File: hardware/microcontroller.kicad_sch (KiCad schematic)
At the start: 8 parts, among them U1 STM32G474QBT6

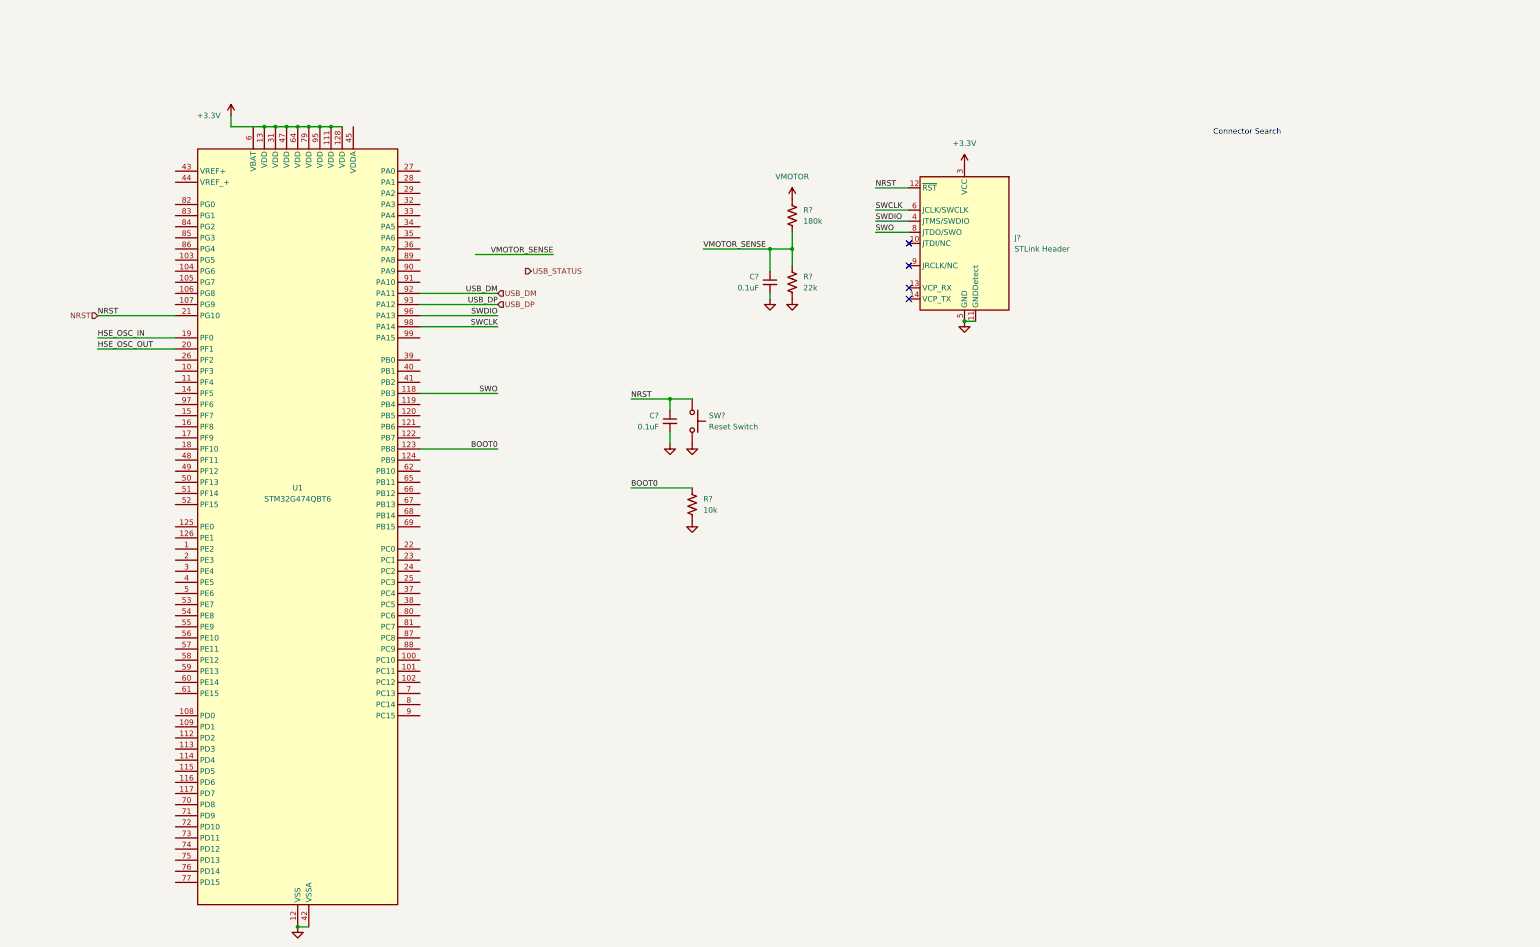
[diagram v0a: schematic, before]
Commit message: SD Card Pull Ups and ESD
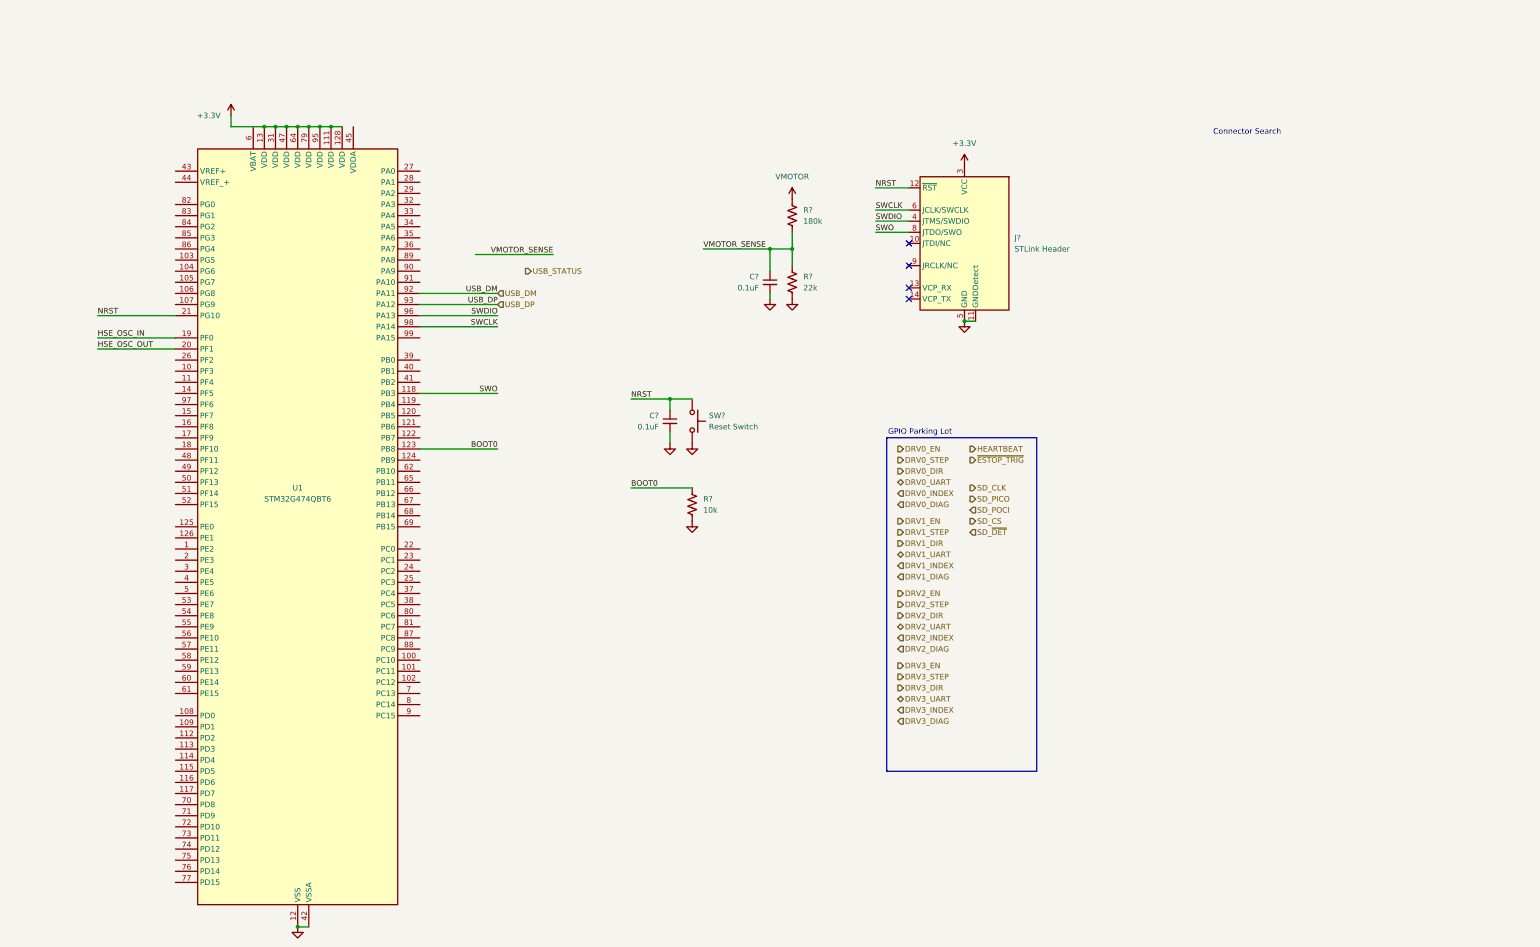
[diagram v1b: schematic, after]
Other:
- note added: "GPIO Parking Lot"

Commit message: Fixes and STM32 Pin Assignment Notes
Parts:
- removed SW?: Reset Switch, Button_Switch_SMD:SW_SPST_PTS647_Sx38, symbol Switch:SW_Push
- added D?: BAT54S, Package_TO_SOT_SMD:SOT-23, symbol Diode:BAT54S
- added R? (x5): 10k, Resistor_SMD:R_0603_1608Metric, symbol Device:R_US
- added SW?: USER3, Button_Switch_SMD:SW_SPST_PTS645Sx43SMTR92, symbol Switch:SW_Push
- added SW?: USER1, Button_Switch_SMD:SW_SPST_PTS645Sx43SMTR92, symbol Switch:SW_Push
- added SW?: USER0, Button_Switch_SMD:SW_SPST_PTS645Sx43SMTR92, symbol Switch:SW_Push
- added SW?: BOOT, Button_Switch_SMD:SW_SPST_PTS645Sx43SMTR92, symbol Switch:SW_Push
- added SW?: USER2, Button_Switch_SMD:SW_SPST_PTS645Sx43SMTR92, symbol Switch:SW_Push
- added SW?: RESET, Button_Switch_SMD:SW_SPST_PTS645Sx43SMTR92, symbol Switch:SW_Push
- C?: value 0.1uF -> 1nF; Part Number CC0603KRX7R9BB104 -> C0603C102K5RACTU; Vendor URL https://www.digikey.com/en/products/detail/yageo/CC0603KRX7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 -> https://www.digikey.com/en/products/detail/kemet/C0603C102K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
- J?: footprint Connector_PinHeader_1.27mm:PinHeader_2x07_P1.27mm_Vertical -> Connector_PinHeader_1.27mm:PinHeader_2x07_P1.27mm_Vertical_SMD; Part Number 3220-14-0100-00 -> FTSH-107-01-L-DV-K-P-TR; Vendor URL https://www.digikey.com/en/products/detail/cnc-tech/3220-14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 -> https://www.digikey.com/en/products/detail/samtec-inc/FTSH-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
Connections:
- net +3.3V: now also U1.6 (VBAT), D?.2 (K), R?.1, R?.1, R?.1, R?.1, R?.1, SW?.1
- net BOOT0: now also SW?.2
- net GND: now also D?.1 (A), SW?.2, SW?.2, SW?.2, SW?.2, SW?.2
- net NRST: now also R?.2, SW?.1
- net VMOTOR_SENSE: now also D?.3 (COM)
- new net USER0: R?.2, SW?.1
- new net USER1: R?.2, SW?.1
- new net USER2: R?.2, SW?.1
- new net USER3: R?.2, SW?.1
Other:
- note added: "Programming/System"
- note added: "STLink v3 Minie connector"
- note added: "Scales max 30.3V down to 3.3V VDDA, safely covering the 29V TMC2209 limit. Node features a Thevenin equivalent resistance (Req) of 19.6kΩ [(180k × 22k) / (180k + 22k)]. Paired with a 1nF capacitor to form an 8.1kHz low-pass filter corner (Tau = 19.6µs, Settling = 98µs). This blocks 20kHz+ TMC2209 chopper noise while reacting fast enough (<100µs) to capture emergency back-EMF spikes. Route directl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"
- note added: "User Buttons"
- note added: "VMOTOR Sense"
- note added: "Would be hard to disconnect cable"
- moved on the sheet: C?, J?, R?, U1

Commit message: Change blue LEDs
Remove extra 5V blue LED driving for simple 3.3V driving instead
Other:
- note added: "FOLLOW ST USB APPNOTE"
